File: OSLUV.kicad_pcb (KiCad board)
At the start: 4 copper layers, 110 x 90 mm, 188 parts, among them IC1 NCP12510ASN65T1G, IC2 SFH6156-3, IC3 INA210, IC4 AP63300WU-7, IC5 AP63300WU-7, IC6 STM32G071KBT6, IC7 TLV9001IDBVR, IC8 FAN3100TSX, J1 B08B-XASK-1-A_LF__SN_, J2 TC2050-IDC, J3 BM02B-SRSS-TB_LF__SN_, J4 BM02B-SRSS-TB_LF__SN_, J5 640445-2, J6 640445-2, J7 B5P-VH, Q1 STD3NK80ZT4, Q2 BAT847B, Q3 BSS138, T1 750343466, T4 NMOS_GDS-KS_SMD, U1 OPA2356AIDGKR, U2 AZ431LANTR, U3 LM2903, U4 AZ431LANTR

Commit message: power parts routed
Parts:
- removed C40, C41: 10u X7R 1210, Capacitor_SMD:C_1210_3225Metric
- moved C54 154.0 mm to (103.0, 109.0)
- moved C51 146.1 mm to (117.8, 123.8)
- moved R50 145.1 mm to (114.8, 123.8)
- moved R54 117.6 mm to (98.1, 120.3), turned to -90 degrees
- moved R55 116.7 mm to (98.1, 115.5), turned to -90 degrees
- moved R56 116.5 mm to (98.1, 110.8), turned to -90 degrees
- moved D17 116.3 mm to (98.0, 104.5), turned to 180 degrees
- moved U1 115.4 mm to (103.2, 106.5), turned to 180 degrees
- moved C55 109.5 mm to (100.6, 120.3), turned to 90 degrees
- moved C56 108.6 mm to (100.6, 115.5), turned to 90 degrees
- moved C57 108.6 mm to (100.3, 110.8), turned to 90 degrees
- moved R57 106.5 mm to (97.6, 107.0), turned to 90 degrees
- moved C58 105.0 mm to (99.1, 107.0), turned to 90 degrees
- moved C43 101.7 mm to (110.0, 113.2)
- moved C42 98.2 mm to (110.3, 111.2)
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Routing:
- net /excimerDriver/VDC_power: track 0.00 -> 40.6 mm
- net /excimerDriver/VDC: track 102.9 -> 71.2 mm
- net /excimerDriver/VDC_filter: track 0.00 -> 27.2 mm
- net GND: track 117.2 -> 100.4 mm
- net +15V: track 0.00 -> 16.5 mm
- net Net-(C25-Pad1): track 0.00 -> 13.7 mm
- net +3V3: track 0.00 -> 11.2 mm
- net Net-(IC5-SW): track 0.00 -> 7.59 mm
- net Net-(IC4-SW): track 0.00 -> 7.52 mm
- net Net-(IC5-FB): track 0.00 -> 4.75 mm
- net Net-(IC4-FB): track 0.00 -> 3.06 mm
- net Net-(IC5-BST): track 0.00 -> 2.69 mm
- net Net-(IC4-BST): track 0.00 -> 1.63 mm
- net Net-(T4-G): track 7.36 -> 6.54 mm

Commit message: 250415_endOfDay
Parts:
- added R65: 1k 0603, Resistor_SMD:R_0603_1608Metric, F.Cu at (194.7, 107.5)
- moved R53 122.4 mm to (55.8, 133.0)
- moved R63 82.2 mm to (103.2, 114.5), turned to 90 degrees
- moved U4 80.3 mm to (108.0, 110.0)
- moved R60 78.9 mm to (105.2, 110.0), turned to 90 degrees
- moved R61 76.5 mm to (104.8, 118.2), turned to 90 degrees
- moved R62 76.4 mm to (106.2, 118.2), turned to 90 degrees
- moved C63 75.0 mm to (103.2, 117.5), turned to -90 degrees
- moved C64 71.8 mm to (110.5, 112.5)
- moved C61 71.1 mm to (107.5, 112.5)
- moved C62 69.6 mm to (107.8, 118.2), turned to -90 degrees
- moved R51 50.3 mm to (124.0, 106.2), turned to 180 degrees
- moved C43 16.8 mm to (126.8, 113.5), turned to 90 degrees
- moved C42 14.9 mm to (125.0, 113.5), turned to 90 degrees
- moved R58 5.10 mm to (105.0, 104.0)
- moved D17 3.82 mm to (101.8, 103.8), turned to 0 degrees
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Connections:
- C51 pad 1: Net-(C51-Pad1) -> /excimerDriver/Isense_MOS
- D15 pad 3: Net-(C51-Pad1) -> /excimerDriver/Isense_MOS
- IC6 pad 12: unconnected-(IC6-PA5-Pad12) -> /excimerDriver/DAC2
- IC6 pad 27: unconnected-(IC6-PD1-Pad27) -> Net-(IC6-PD1)
- IC6 pad 28: unconnected-(IC6-PD2-Pad28) -> /excimerDriver/Isense_MOS
- IC6 pad 30: unconnected-(IC6-PB6-Pad30) -> /excimerDriver/UV_LED
- IC6 pad 31: unconnected-(IC6-PB7-Pad31) -> /excimerDriver/MCU_RX
- R50 pad 2: Net-(C51-Pad1) -> /excimerDriver/Isense_MOS
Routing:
- net /excimerDriver/lampDriver/HV_Drain: track 0.00 -> 26.7 mm
- net /excimerDriver/Isense_MOS: track 0.00 -> 19.6 mm
- net Net-(U1B-+): track 0.00 -> 11.1 mm
- net Net-(D17-K): track 0.00 -> 8.56 mm
- net Net-(U1A-+): track 0.00 -> 6.32 mm
- net Net-(D17-A): track 0.00 -> 4.52 mm
- net Net-(R48-Pad2): track 0.00 -> 2.05 mm
- net /excimerDriver/Usense_Lamp: track 0.00 -> 0.65 mm

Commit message: old current control design
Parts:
- moved D16 56.4 mm to (52.0, 131.8)
- moved J7 5.03 mm to (54.2, 117.8)
- moved R51 2.02 mm to (122.0, 106.5)
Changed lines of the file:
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@@
 	(footprint "Hansmann:CONN_B2P5-VH_JST"
 		(layer "F.Cu")
-		(at 54 122.839999 90)
+		(at 54.2455 117.8151 90)
 		(tags "B5P-VH ")
 		(property "Reference" "J7"
@@
 	(footprint "Resistor_SMD:R_0603_1608Metric"
 		(layer "F.Cu")
-		(at 124 106.25 180)
+		(at 122 106.5 180)
 		(descr "Resistor SMD 0603 (1608 Metric), square (rectangular) end terminal, IPC-7351 nominal, (Body size source: IPC-SM-782 page 72, https://www.pcb-3d.com/wordpress/wp-content/uploads/ipc-sm-782a_amendment_1_and_2.pdf), generated with kicad-footprint-generator")
 		(tags "resistor")
@@
 	(footprint "Package_TO_SOT_SMD:SOT-23"
 		(layer "F.Cu")
-		(at 105.92 148.405)
+		(at 52 131.75)
 		(descr "SOT, 3 Pin (JEDEC TO-236 Var AB https://www.jedec.org/document_search?search_api_views_fulltext=TO-236), generated with kicad-footprint-generator ipc_gullwing_generator.py")
 		(tags "SOT TO_SOT_SMD")

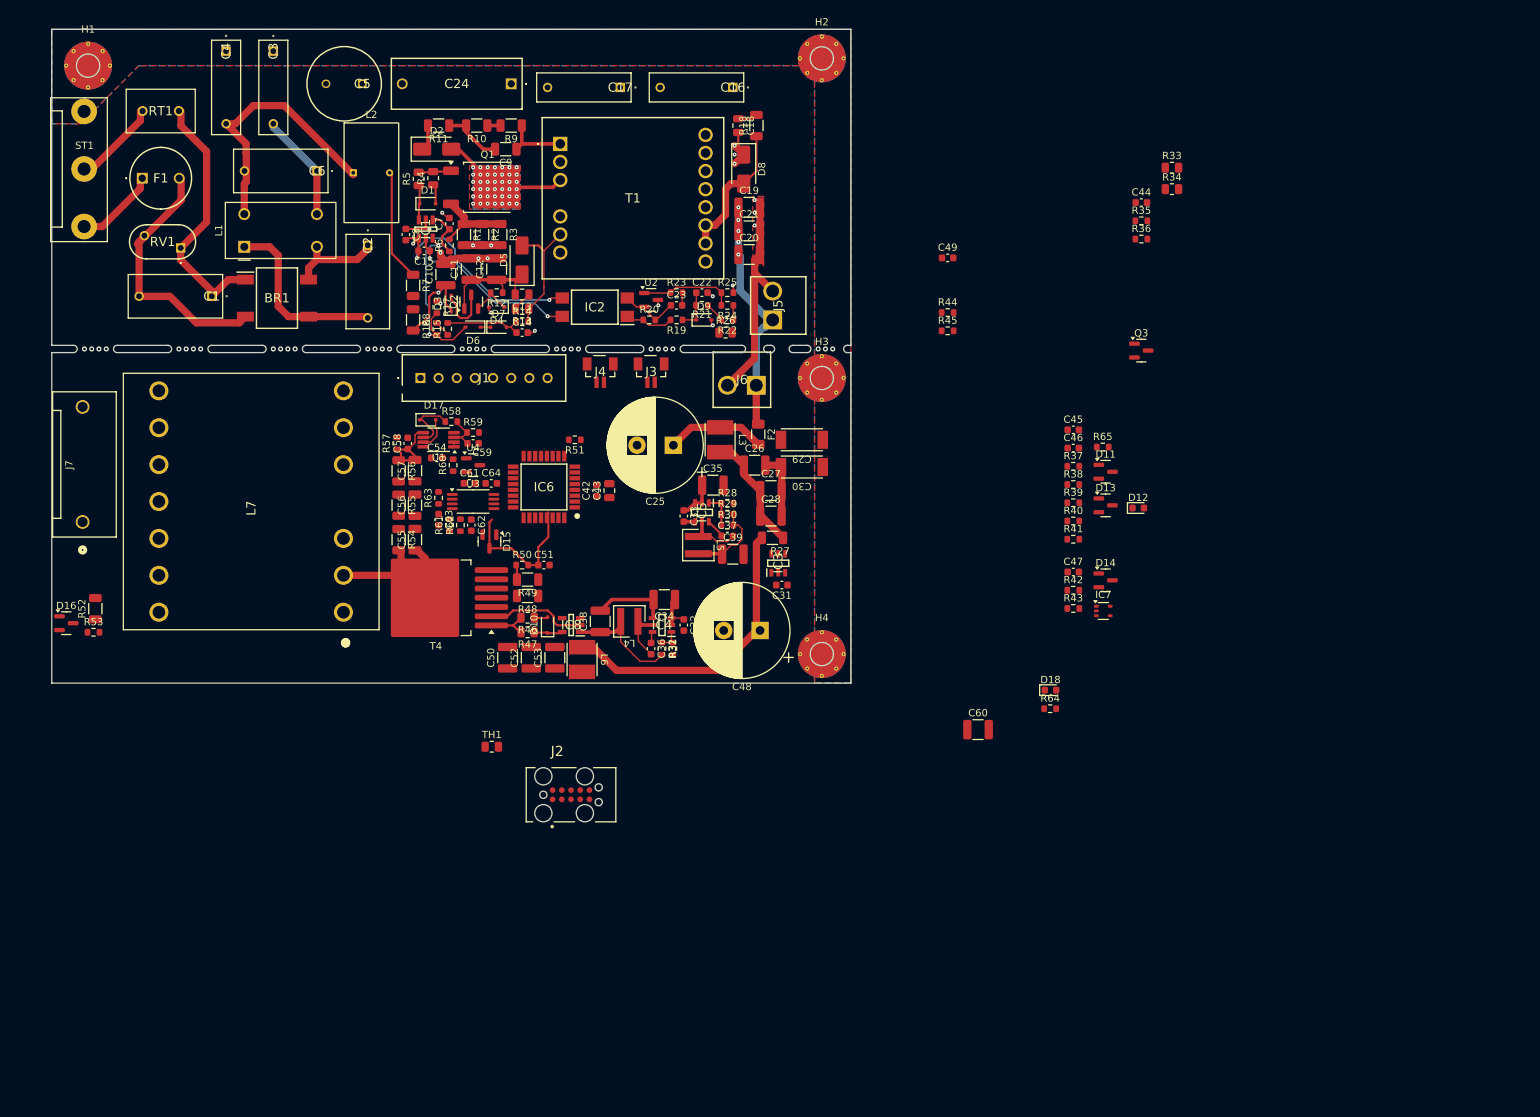
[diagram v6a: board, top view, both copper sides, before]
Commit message: new current control V1
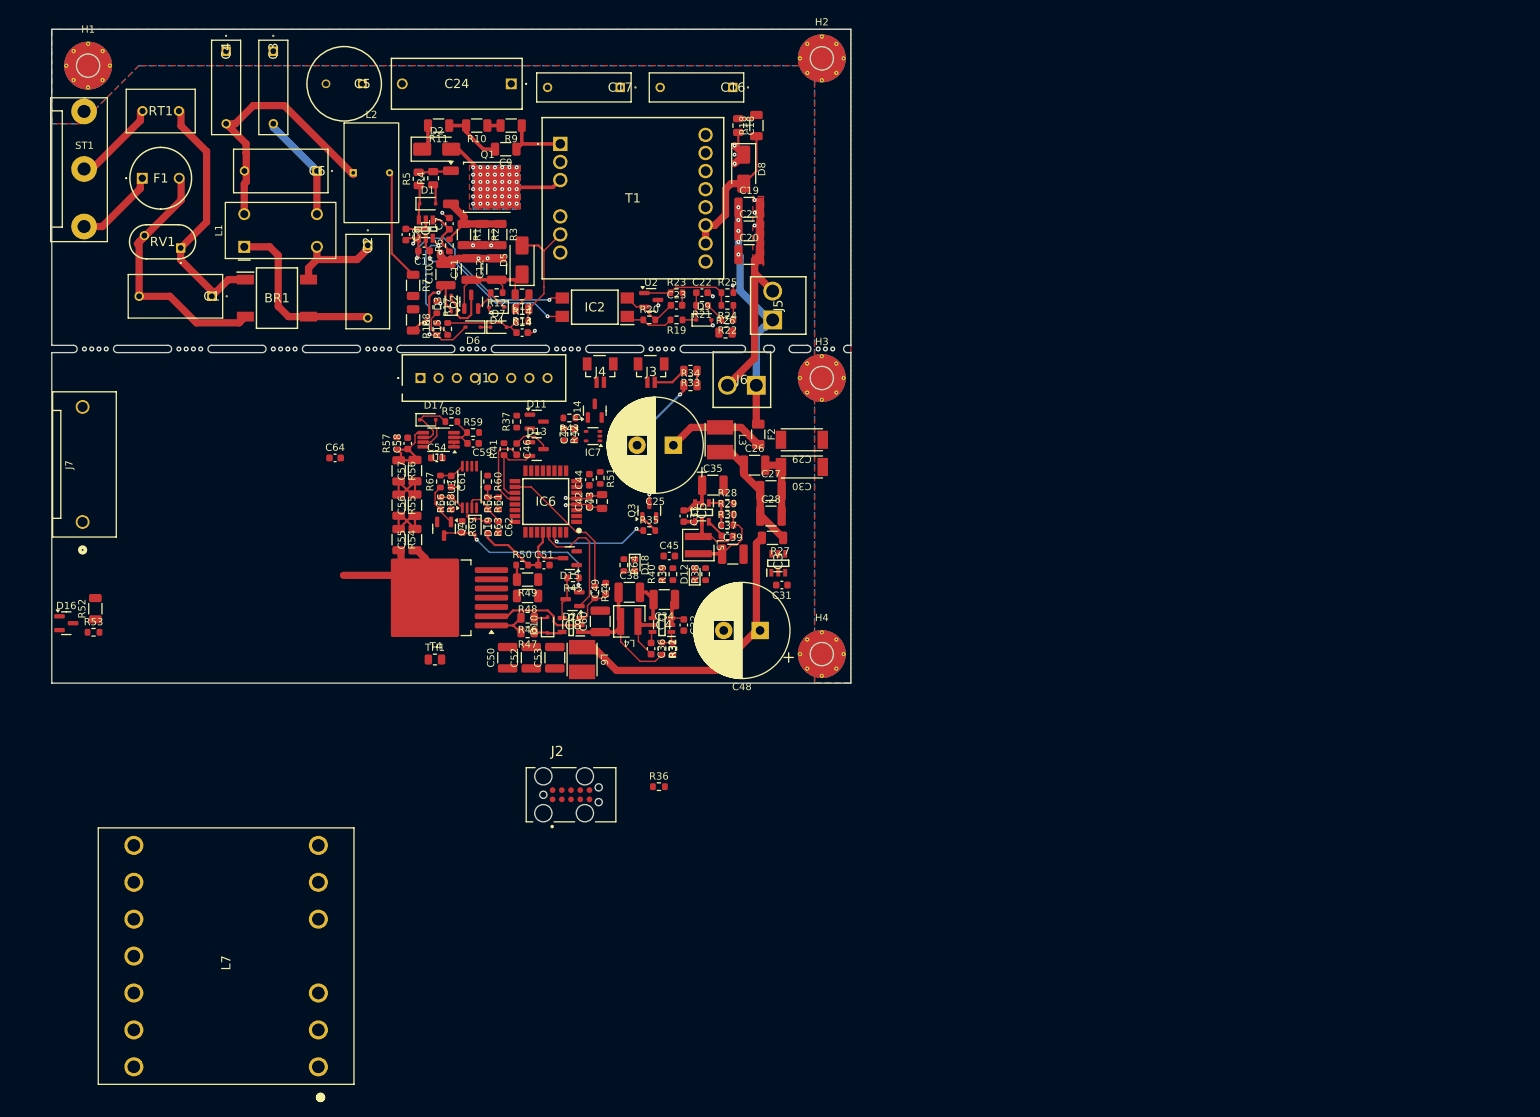
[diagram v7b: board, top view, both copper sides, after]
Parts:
- removed C63: 100p 0603, Capacitor_SMD:C_0603_1608Metric
- removed R65: 1k 0603, Resistor_SMD:R_0603_1608Metric
- removed U4: AZ431LANTR, Package_TO_SOT_SMD:SOT-23
- added D19: BAT54J, Diode_SMD:D_SOD-323F, F.Cu at (108.2, 118.5)
- added D20: BAS40-05, Package_TO_SOT_SMD:SOT-23, F.Cu at (121.7, 128.4)
- added Q4: BC807, Package_TO_SOT_SMD:SOT-23, F.Cu at (104.0, 118.8)
- added R66: 10k 0603, Resistor_SMD:R_0603_1608Metric, F.Cu at (105.0, 115.2)
- added R67: 10k 0603, Resistor_SMD:R_0603_1608Metric, F.Cu at (103.5, 112.2)
- added R68: 10k 0603, Resistor_SMD:R_0603_1608Metric, F.Cu at (103.5, 115.2)
- added R69: 100k 0603, Resistor_SMD:R_0603_1608Metric, F.Cu at (106.5, 118.5)
- R45: value 10k 0603 -> 100k 0603
- R61: value 10k 0603 -> 1k 0603
- R62: value 10k 0603 -> 2k2 0603
- R63: value 1k 0603 -> 10k 0603
- moved R36 100.5 mm to (133.6, 154.2)
- moved C44 85.0 mm to (124.0, 112.0), turned to 90 degrees
- moved R35 80.0 mm to (132.2, 119.0)
- moved R41 79.3 mm to (112.2, 107.8), turned to 90 degrees
- moved D13 78.7 mm to (116.8, 107.8)
- moved D11 78.6 mm to (116.8, 104.0)
- moved R37 76.9 mm to (114.0, 104.0), turned to 90 degrees
- moved C46 76.6 mm to (114.0, 107.8), turned to -90 degrees
- moved IC7 74.3 mm to (124.5, 106.0), turned to 180 degrees
- moved R43 74.2 mm to (121.2, 103.5), turned to 180 degrees
- moved D14 74.1 mm to (124.8, 102.5), turned to 90 degrees
- moved R42 73.3 mm to (120.5, 105.8), turned to -90 degrees
- moved R33 71.9 mm to (137.9, 97.0), turned to 180 degrees
- moved R34 71.6 mm to (137.9, 99.0)
- moved Q3 71.2 mm to (132.2, 116.2), turned to 90 degrees
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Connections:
- C62 pad 1: Net-(U4-K) -> Net-(U3A-+)
- IC6 pad 27: Net-(IC6-PD1) -> unconnected-(IC6-PD1-Pad27)
- IC6 pad 29: unconnected-(IC6-PD3-Pad29) -> /excimerDriver/DRV_Mask
- R60 pad 2: Net-(U4-K) -> Net-(R60-Pad2)
- R61 pad 1: Net-(U4-K) -> Net-(R60-Pad2)
- R62 pad 2: Net-(U3A-+) -> Net-(R60-Pad2)
- U3 pad 7: /excimerDriver/PeakCurrent -> unconnected-(U3-Pad7)
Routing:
- net Net-(D19-A): track 0.00 -> 24.7 mm, vias 0 -> 2
- net /excimerDriver/DRV: track 0.00 -> 20.3 mm
- net Net-(Q3-D): track 0.00 -> 18.3 mm, vias 0 -> 2
- net /excimerDriver/DRV_Mask: track 0.00 -> 17.2 mm
- net /excimerDriver/UV_LED: track 0.00 -> 14.3 mm, vias 0 -> 2
- net /excimerDriver/AlivePWM: track 0.00 -> 11.0 mm
- net Net-(IC6-PA9): track 0.00 -> 10.4 mm
- net Net-(C55-Pad2): track 0.00 -> 9.63 mm
- net Net-(C56-Pad2): track 0.00 -> 9.58 mm
- net +3V3: track 11.2 -> 20.1 mm, vias 0 -> 1
- net Net-(U3A-+): track 0.00 -> 6.62 mm
- net Net-(Q4-B): track 0.00 -> 6.03 mm
- net Net-(D20-K): track 0.00 -> 5.83 mm
- net Net-(IC8-IN+): track 0.00 -> 5.69 mm
- net Net-(C46-Pad1): track 0.00 -> 5.15 mm
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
